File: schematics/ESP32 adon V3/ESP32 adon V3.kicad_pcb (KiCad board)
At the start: 2 copper layers, 42.5 x 63.1 mm, 38 parts, among them J1 Conn_01x08_Pin, J2 Conn_01x08_Pin, J3 Conn_01x02_Pin, J4 Conn_01x08_Pin, J5 Conn_01x08_Pin, J6 USB4215-03-A_REVA, J7 Conn_01x04_Pin, J8 Conn_01x02_Pin, Q4 MMBT7002K, Q5 MMBT7002K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

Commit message: update de schematics
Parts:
- removed C1, C2, C3, C4, C5, C6: 1µF, Capacitor_SMD:C_0603_1608Metric
- removed D1, D2: CMMSH1-60G TR PBFREE, Diode_SMD:D_SOD-123F
- removed D3: SMF05C.TCT, Package_TO_SOT_SMD:Vishay_PowerPAK_SC70-6L_Dual
- removed J1, J2, J4, J5: Conn_01x08_Pin, Connector_PinSocket_2.54mm:PinSocket_1x08_P2.54mm_Vertical
- removed J3: Conn_01x02_Pin, Connector_PinSocket_2.54mm:PinSocket_1x02_P2.54mm_Vertical
- removed J6: USB4215-03-A_REVA, Connector_USB:usb4215-3472997
- removed J7: Conn_01x04_Pin, Connector_PinSocket_2.54mm:PinSocket_1x04_P2.54mm_Vertical
- removed J8: Conn_01x02_Pin, Resistor_SMD:R_0603_1608Metric_Pad0.98x0.95mm_HandSolder
- removed MT1: ICM-42670-P, Package_LGA:Bosch_LGA-14_3x2.5mm_P0.5mm
- removed Q4, Q5, Q6: MMBT7002K, Package_TO_SOT_SMD:SOT-23
- removed R1, R18, R3, R4, R5, R6, R7, R8: 10K, Resistor_SMD:R_0603_1608Metric
- removed R16, R17: 5.1k, Resistor_SMD:R_0603_1608Metric
- removed R2: 20K, Resistor_SMD:R_0603_1608Metric
- removed SW2: SW_Push, Button_Switch_THT:SW_PUSH_6mm
- removed U1: ESP32-C6-WROOM-1, PCM_Espressif:ESP32-C6-WROOM-1
- removed U2: TCA9535DBR, Package_SO:TSSOP-24_4.4x7.8mm_P0.65mm
- removed U3: ADS1115IDGS, Package_SO:TSSOP-10_3x3mm_P0.5mm
- removed U4: TLV75733PDBV, Package_TO_SOT_SMD:SOT-23-5
- removed U6: MLX90395KDC-BBA-101-RE, Package_SO:SOIC-8_3.9x4.9mm_P1.27mm
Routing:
- net +3.3V: track 117.8 -> 0.00 mm, vias 6 -> 0
- net +5V: track 106.7 -> 0.00 mm, vias 2 -> 0
- net /SDA_{5V}: track 100.1 -> 0.00 mm, vias 9 -> 0
- net /SCL_{5V}: track 98.4 -> 0.00 mm, vias 9 -> 0
- net /SDA_{3.3V}: track 57.9 -> 0.00 mm, vias 1 -> 0
- net /SCL_{3.3V}: track 53.5 -> 0.00 mm, vias 1 -> 0
- net Net-(Q4-S): track 50.4 -> 0.00 mm, vias 4 -> 0
- net Net-(U1-U0RXD/GPIO17): track 42.5 -> 0.00 mm, vias 2 -> 0
- net /D-: track 36.8 -> 0.00 mm, vias 3 -> 0
- net /D+: track 36.3 -> 0.00 mm, vias 3 -> 0
- net Net-(J4-Pin_4): track 35.1 -> 0.00 mm, vias 1 -> 0
- net Net-(J4-Pin_3): track 33.7 -> 0.00 mm, vias 1 -> 0
- net Net-(J4-Pin_2): track 32.4 -> 0.00 mm, vias 1 -> 0
- net Net-(J4-Pin_1): track 31.2 -> 0.00 mm, vias 2 -> 0
- net +5Vin: track 30.8 -> 0.00 mm, vias 4 -> 0
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- removed copper zone on F.Cu, net +3.3V
- removed copper zone on B.Cu, net +5Vin
- removed copper zone on B.Cu, net /Vin_reg
- removed copper zone on F.Cu, net /Vin_reg
- removed copper zone on B.Cu, net GND
- removed copper zone on F.Cu, net GND
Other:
- board outline removed
- board text removed: "ontworpen door Stan Debakker"

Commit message: begin al met het tekenen van ESP32 addon V3
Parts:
- added C1: 1µF, Capacitor_SMD:C_0603_1608Metric, F.Cu at (153.8, 52.8)
- added C2: 1µF, Capacitor_SMD:C_0603_1608Metric, F.Cu at (60.6, 32.6)
- added C3: 1µF, Capacitor_SMD:C_0603_1608Metric, F.Cu at (153.8, 57.8)
- added C4: 1µF, Capacitor_SMD:C_0603_1608Metric, F.Cu at (62.4, 32.6)
- added C5: 1µF, Capacitor_SMD:C_0603_1608Metric, F.Cu at (85.0, 39.6)
- added C6: 1µF, Capacitor_SMD:C_0603_1608Metric, F.Cu at (153.8, 65.3)
- added D1: CMMSH1-60G TR PBFREE, Diode_SMD:D_SOD-123F, F.Cu at (154.6, 68.2)
- added D2: CMMSH1-60G TR PBFREE, Diode_SMD:D_SOD-123F, F.Cu at (154.6, 71.6)
- added J1: Conn_01x08_Pin, Connector_PinSocket_2.54mm:PinSocket_1x08_P2.54mm_Vertical, F.Cu at (51.8, 31.8)
- added J10: Conn_01x01, Connector_Wire:SolderWirePad_1x01_SMD_1x2mm, F.Cu at (59.8, 56.0)
- added J11: Conn_01x01, Connector_Wire:SolderWirePad_1x01_SMD_1x2mm, F.Cu at (87.5, 40.3)
- added J12: Conn_01x01, Connector_Wire:SolderWirePad_1x01_SMD_1x2mm, F.Cu at (139.0, 89.3)
- added J13: Conn_01x01, Connector_Wire:SolderWirePad_1x01_SMD_1x2mm, F.Cu at (141.3, 89.3)
- added J14: Conn_01x01, Connector_Wire:SolderWirePad_1x01_SMD_1x2mm, F.Cu at (143.7, 89.3)
- added J2: Conn_01x08_Pin, Connector_PinSocket_2.54mm:PinSocket_1x08_P2.54mm_Vertical, F.Cu at (51.8, 69.6)
- added J3: Conn_01x02_Pin, Connector_PinSocket_2.54mm:PinSocket_1x02_P2.54mm_Vertical, F.Cu at (72.3, 91.4)
- added J4: Conn_01x08_Pin, Connector_PinSocket_2.54mm:PinSocket_1x08_P2.54mm_Vertical, F.Cu at (90.3, 69.6)
- added J5: Conn_01x08_Pin, Connector_PinSocket_2.54mm:PinSocket_1x08_P2.54mm_Vertical, F.Cu at (90.3, 31.8)
- added J6: USB4215-03-A_REVA, Connector_USB:usb4215-3472997, F.Cu at (92.0, 58.6)
- added J7: Conn_01x04_Pin, Connector_PinSocket_2.54mm:PinSocket_1x04_P2.54mm_Vertical, F.Cu at (147.9, 59.1)
- added J9: Conn_01x04_Pin, Connector_PinSocket_2.54mm:PinSocket_1x04_P2.54mm_Vertical, F.Cu at (148.0, 72.5)
- added MT1: ICM-42670-P, Package_LGA:Bosch_LGA-14_3x2.5mm_P0.5mm, F.Cu at (172.7, 47.8)
- added Q1: MMBT7001K, Package_TO_SOT_SMD:TSOT-23, F.Cu at (142.9, 59.3)
- added Q2: MMBT7001K, Package_TO_SOT_SMD:TSOT-23, F.Cu at (142.9, 63.9)
- added Q3: MMBT7001K, Package_TO_SOT_SMD:TSOT-23, F.Cu at (142.9, 68.6)
- added R1: 10K, Resistor_SMD:R_0603_1608Metric, F.Cu at (157.8, 52.8)
- added R16: 5.1k, Resistor_SMD:R_0603_1608Metric, F.Cu at (82.4, 61.8)
- added R17: 5.1k, Resistor_SMD:R_0603_1608Metric, F.Cu at (82.4, 55.4)
- added R18: 10K, Resistor_SMD:R_0603_1608Metric, F.Cu at (58.4, 32.6)
- added R2: 20K, Resistor_SMD:R_0603_1608Metric, F.Cu at (157.8, 55.3)
- added R3: 10K, Resistor_SMD:R_0603_1608Metric, F.Cu at (157.8, 57.8)
- added R4: 10K, Resistor_SMD:R_0603_1608Metric, F.Cu at (157.8, 60.3)
- added R5: 10K, Resistor_SMD:R_0603_1608Metric, F.Cu at (157.8, 62.8)
- added R6: 10K, Resistor_SMD:R_0603_1608Metric, F.Cu at (157.8, 65.3)
- added R7: 10K, Resistor_SMD:R_0603_1608Metric, F.Cu at (161.9, 52.8)
- added R8: 10K, Resistor_SMD:R_0603_1608Metric, F.Cu at (161.9, 55.3)
- added SW2: SW_Push, Button_Switch_THT:SW_PUSH_6mm, F.Cu at (57.3, 42.3)
- added U1: ESP32-C6-WROOM-1, PCM_Espressif:ESP32-C6-WROOM-1, F.Cu at (73.2, 39.8)
- added U2: TCA9535DBR, Package_SO:TSSOP-24_4.4x7.8mm_P0.65mm, F.Cu at (55.0, 58.6)
- added U3: ADS1115IDGS, Package_SO:TSSOP-10_3x3mm_P0.5mm, F.Cu at (86.5, 35.6)
- added U4: TLV75733PDBV, Package_TO_SOT_SMD:SOT-23-5, F.Cu at (172.8, 31.5)
- added U5: USBLC6-2SC6, Package_TO_SOT_SMD:SOT-23-6, F.Cu at (81.1, 58.6)
- added U6: MLX90395KDC-BBA-101-RE, Package_SO:SOIC-8_3.9x4.9mm_P1.27mm, F.Cu at (135.3, 69.5)
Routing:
- net +5Vin: track 0.00 -> 29.7 mm
- net Net-(J1-Pin_1): track 0.00 -> 25.9 mm
- net Net-(J1-Pin_2): track 0.00 -> 23.1 mm
- net Net-(J1-Pin_3): track 0.00 -> 20.3 mm
- net Net-(J1-Pin_4): track 0.00 -> 17.5 mm
- net Net-(U1-EN/CHIP_PU): track 0.00 -> 15.0 mm
- net Net-(J1-Pin_5): track 0.00 -> 14.7 mm
- net Net-(J1-Pin_6): track 0.00 -> 12.0 mm
- net Net-(J1-Pin_7): track 0.00 -> 9.29 mm
- net +3.3V: track 0.00 -> 7.95 mm
- net Net-(J1-Pin_8): track 0.00 -> 6.25 mm
- net Net-(J6-DP1): track 0.00 -> 5.90 mm
- net Net-(J6-DN1): track 0.00 -> 5.85 mm
- net Net-(J6-CC1): track 0.00 -> 3.41 mm
- net Net-(J6-CC2): track 0.00 -> 3.21 mm
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- added copper zone on F.Cu, net +3.3V
- added copper zone on F.Cu, net +5Vin
- added copper zone on B.Cu, net GND
- added copper zone on F.Cu, net GND
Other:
- board outline added: 42 x 63.1 mm

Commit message: verder tekenen en datasheets controleren
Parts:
- moved C6 92.2 mm to (64.9, 89.6), turned to 90 degrees
- moved J12 83.5 mm to (55.5, 91.5), turned to 90 degrees
- moved U6 77.5 mm to (60.5, 89.6)
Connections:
- U6 pad 3: unconnected-(U6-MISO-Pad3) -> GND
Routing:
- net Net-(J2-Pin_8): track 0.00 -> 27.7 mm
- net Net-(J2-Pin_7): track 0.00 -> 25.0 mm
- net Net-(J2-Pin_6): track 0.00 -> 22.3 mm
- net Net-(J2-Pin_5): track 0.00 -> 19.6 mm
- net Net-(J2-Pin_4): track 0.00 -> 16.9 mm
- net Net-(J2-Pin_3): track 0.00 -> 14.2 mm
- net Net-(J2-Pin_2): track 0.00 -> 11.6 mm
- net Net-(J2-Pin_1): track 0.00 -> 8.29 mm
- net +5V: track 0.00 -> 6.09 mm
- net Net-(J5-Pin_1): track 0.00 -> 4.50 mm
- net Net-(J5-Pin_4): track 0.00 -> 4.39 mm
- net Net-(J5-Pin_2): track 0.00 -> 3.16 mm
- net Net-(J5-Pin_3): track 0.00 -> 3.16 mm
- net Net-(J11-Pin_1): track 0.00 -> 3.12 mm
- net Net-(J12-Pin_1): track 0.00 -> 2.50 mm
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- added copper zone on F.Cu, net +5V
- added copper zone on F.Cu, net Net-(J10-Pin_1)

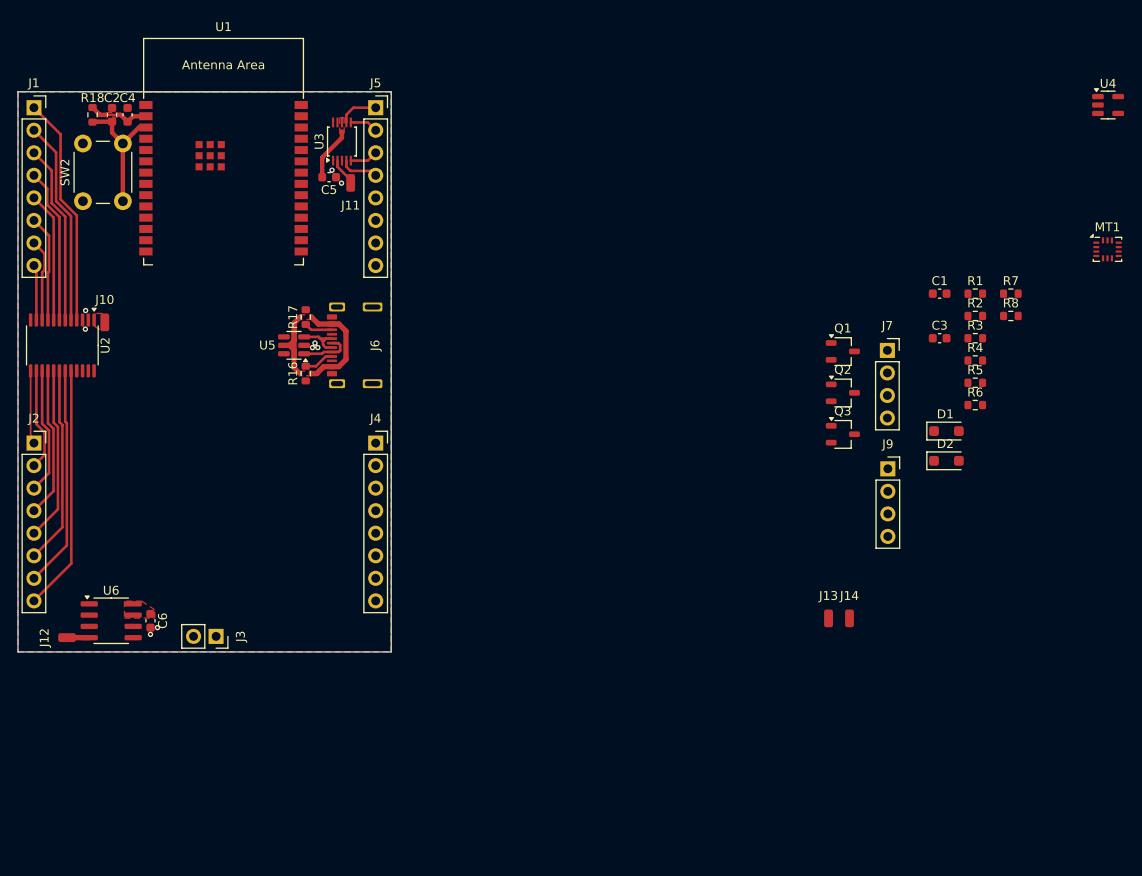
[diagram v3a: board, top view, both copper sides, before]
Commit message: voeg de imu en de 3.3V I²C conectoren toe
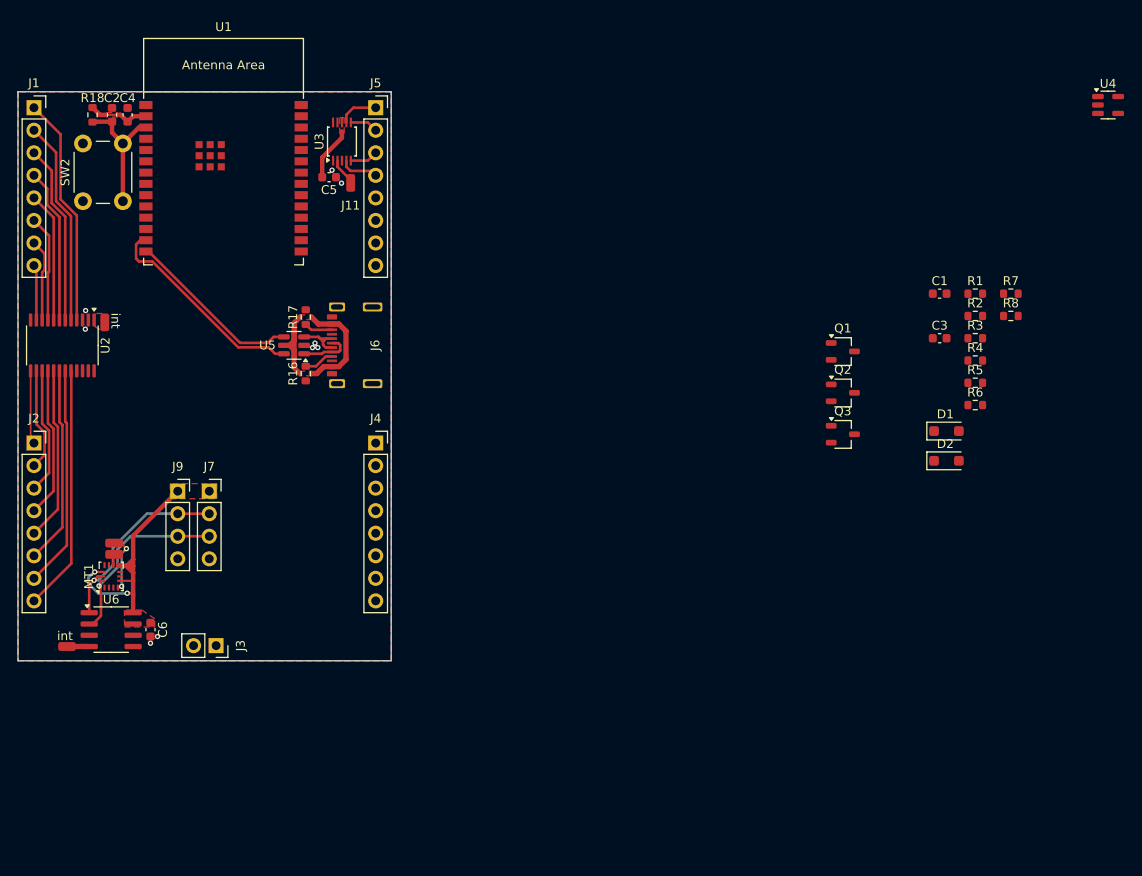
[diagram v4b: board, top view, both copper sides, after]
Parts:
- moved MT1 118.1 mm to (60.5, 84.6), turned to 90 degrees
- moved Jd 83.2 mm to (60.8, 82.1), turned to 90 degrees
- moved J13 80.9 mm to (60.8, 80.8), turned to 90 degrees
- moved J9 80.0 mm to (68.0, 75.0)
- moved J7 78.0 mm to (71.5, 75.0)
- moved J3 1.04 mm to (72.3, 92.4)
- moved C6 1.00 mm to (64.9, 90.6)
- moved J12 1.00 mm to (55.5, 92.5)
- moved U6 1.00 mm to (60.5, 90.6)
- renumbered J14 to Jd
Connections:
- MT1 pad 2: unconnected-(MT1-RESV-Pad10) -> GND
- MT1 pad 3: unconnected-(MT1-RESV-Pad10)_1 -> GND
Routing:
- net +3.3V: track 7.95 -> 37.2 mm, vias 0 -> 2
- net /D-: track 0.00 -> 24.0 mm
- net /SCL_{3.3V}: track 0.00 -> 22.3 mm, vias 0 -> 1
- net /SDA_{3.3V}: track 0.00 -> 22.0 mm, vias 0 -> 1
- net /D+: track 0.00 -> 20.3 mm
- net Net-(J13-Pin_1): track 0.00 -> 6.61 mm, vias 0 -> 2
- net Net-(J14-Pin_1): track 0.00 -> 1.25 mm
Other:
- board size 42 x 63.1 mm -> 42 x 64.1 mm
- board text added: "int"

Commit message: zet alle componenten op de juist plaats en alles is al verbonden
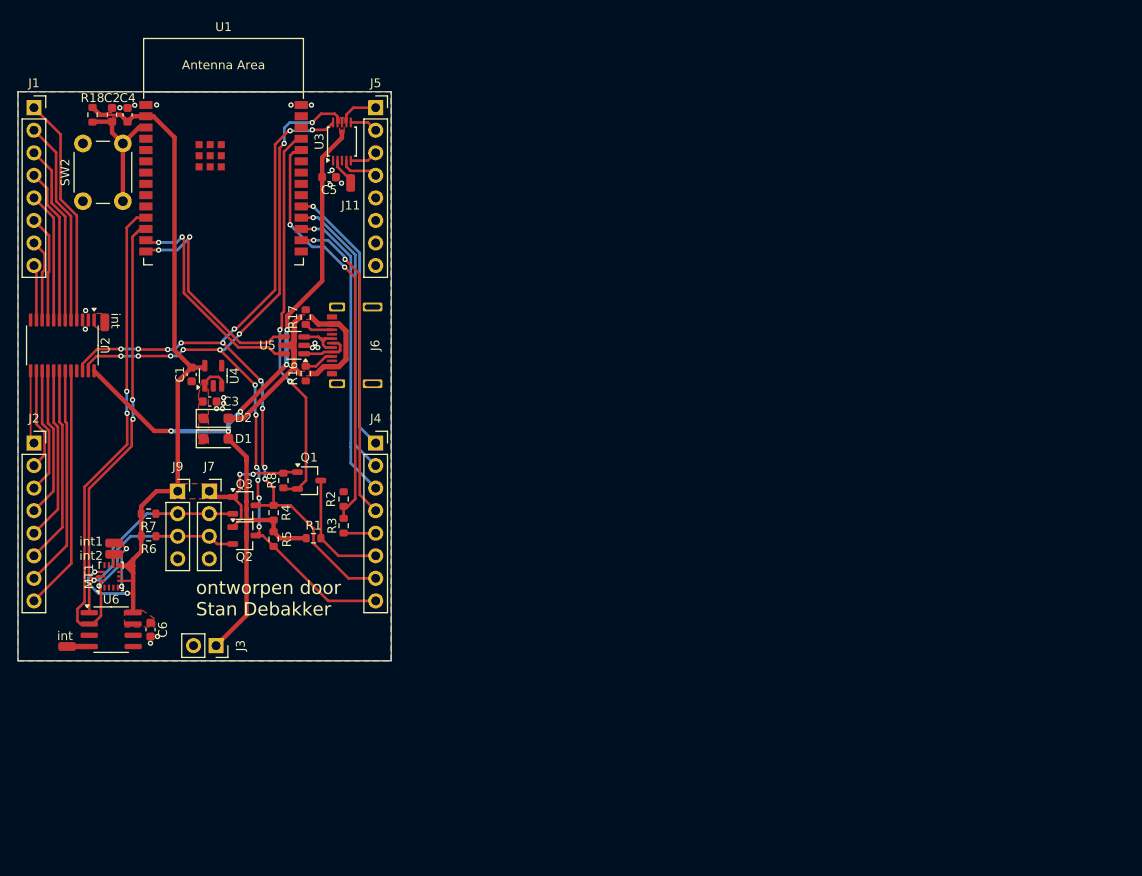
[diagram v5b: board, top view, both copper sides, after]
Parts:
- removed Jd: Conn_01x01, Connector_Wire:SolderWirePad_1x01_SMD_1x2mm
- added J14: Conn_01x01, Connector_Wire:SolderWirePad_1x01_SMD_1x2mm, F.Cu at (60.8, 82.1)
- moved U4 105.3 mm to (72.0, 62.0), turned to 90 degrees
- moved R7 100.3 mm to (64.7, 77.5), turned to 180 degrees
- moved R6 94.3 mm to (64.7, 80.1), turned to 180 degrees
- moved C1 84.8 mm to (69.6, 61.9), turned to -90 degrees
- moved R8 84.0 mm to (79.9, 73.8), turned to -90 degrees
- moved C3 82.5 mm to (71.6, 64.9)
- moved D2 82.4 mm to (72.3, 66.8)
- moved D1 82.3 mm to (72.3, 69.1)
- moved R5 81.0 mm to (78.8, 80.4), turned to 90 degrees
- moved R4 80.9 mm to (78.8, 77.4), turned to -90 degrees
- moved R1 79.5 mm to (83.3, 80.3)
- moved R3 74.2 mm to (86.7, 78.9), turned to -90 degrees
- moved R2 74.1 mm to (86.7, 75.9), turned to 90 degrees
- moved Q2 69.3 mm to (75.5, 80.0)
- moved Q3 67.9 mm to (75.5, 76.6)
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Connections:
- MT1 pad 2: GND -> unconnected-(MT1-RESV-Pad10)
- MT1 pad 3: GND -> unconnected-(MT1-RESV-Pad10)_1
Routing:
- net /SDA_{5V}: track 0.00 -> 91.5 mm, vias 0 -> 14
- net /SCL_{5V}: track 0.00 -> 88.7 mm, vias 0 -> 12
- net +5V: track 6.09 -> 93.5 mm, vias 0 -> 5
- net +3.3V: track 37.2 -> 102.3 mm, vias 2 -> 4
- net /SDA_{3.3V}: track 22.0 -> 78.2 mm, vias 1 -> 3
- net /SCL_{3.3V}: track 22.3 -> 70.3 mm, vias 1 -> 3
- net Net-(U1-U0RXD/GPIO17): track 0.00 -> 47.7 mm, vias 0 -> 2
- net Net-(Q1-S): track 0.00 -> 44.0 mm, vias 0 -> 2
- net Net-(J4-Pin_4): track 0.00 -> 35.7 mm, vias 0 -> 2
- net Net-(J4-Pin_3): track 0.00 -> 34.1 mm, vias 0 -> 1
- net Net-(J4-Pin_2): track 0.00 -> 32.5 mm, vias 0 -> 1
- net Net-(J4-Pin_1): track 0.00 -> 30.9 mm, vias 0 -> 1
- net /TX: track 0.00 -> 13.5 mm
- net +5Vin: track 29.7 -> 39.5 mm
- net /D+: track 20.3 -> 25.8 mm, vias 0 -> 2
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- added copper zone on F.Cu, net /Vin_reg
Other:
- board text added: "int1 int2"
- board text added: "ontworepen door Stan Debakker"
- board text added: "ontworpen door Stan Debakker"

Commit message: heatsikn voor de ESP32 maken
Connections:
- MT1 pad 2: unconnected-(MT1-RESV-Pad10) -> GND
- MT1 pad 3: unconnected-(MT1-RESV-Pad10)_1 -> GND
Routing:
- net GND: vias 19 -> 78

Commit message: controller ESP32 addon V3
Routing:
- net /SCL_{5V}: track 88.7 -> 88.8 mm, vias 12 -> 10
- net /SDA_{5V}: track 91.5 -> 91.4 mm, vias 14 -> 12
- net GND: vias 78 -> 126
